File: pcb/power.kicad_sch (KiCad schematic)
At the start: 27 parts, among them IC3 XC6227C331MR-G, IC6 BQ24073RGTR, U3 CR2032-BS-6-1

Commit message: created step file
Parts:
- removed R27: DNF_0805, Resistor_SMD:R_0805_2012Metric_Pad1.20x1.40mm_HandSolder, symbol personal:DNF_0805
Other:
- note removed: "Charger Bypass"
- note removed: "Remove Charger 0 Ohm link first!"

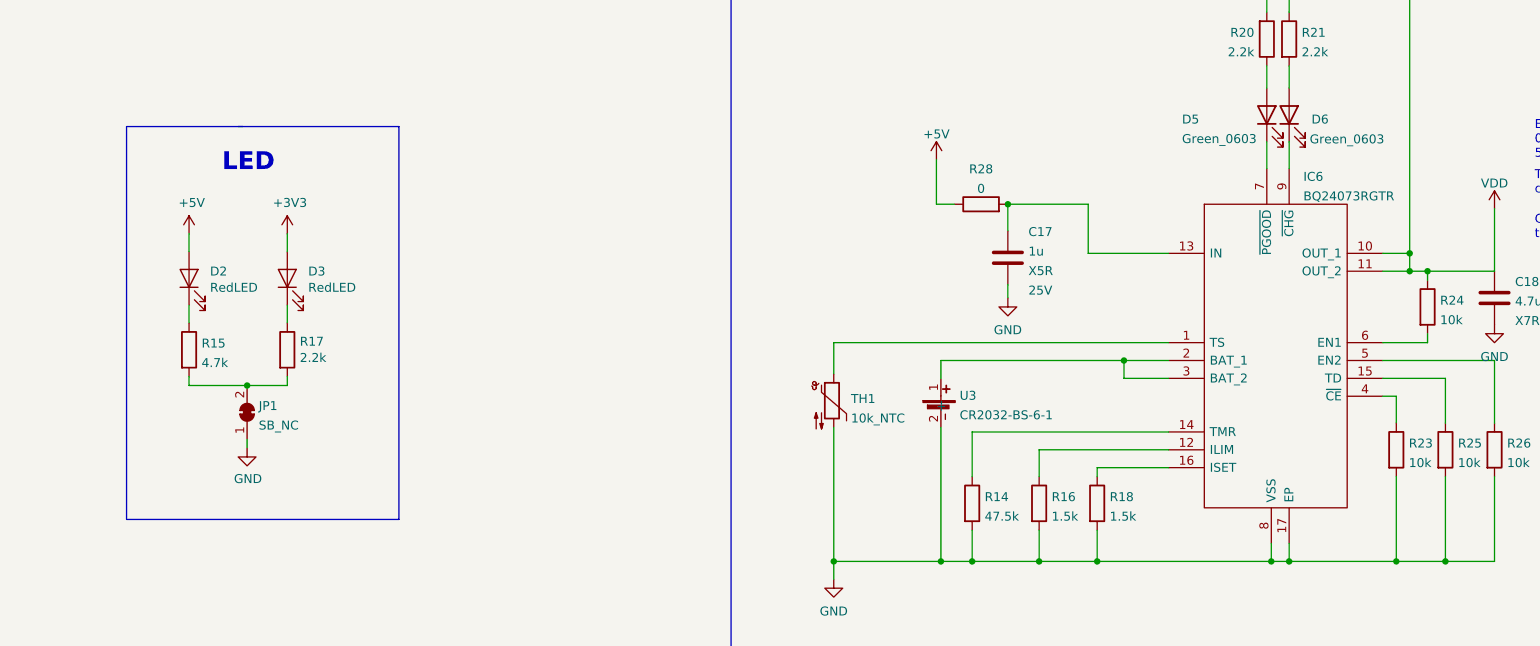
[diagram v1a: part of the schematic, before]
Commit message: Added demo scripts
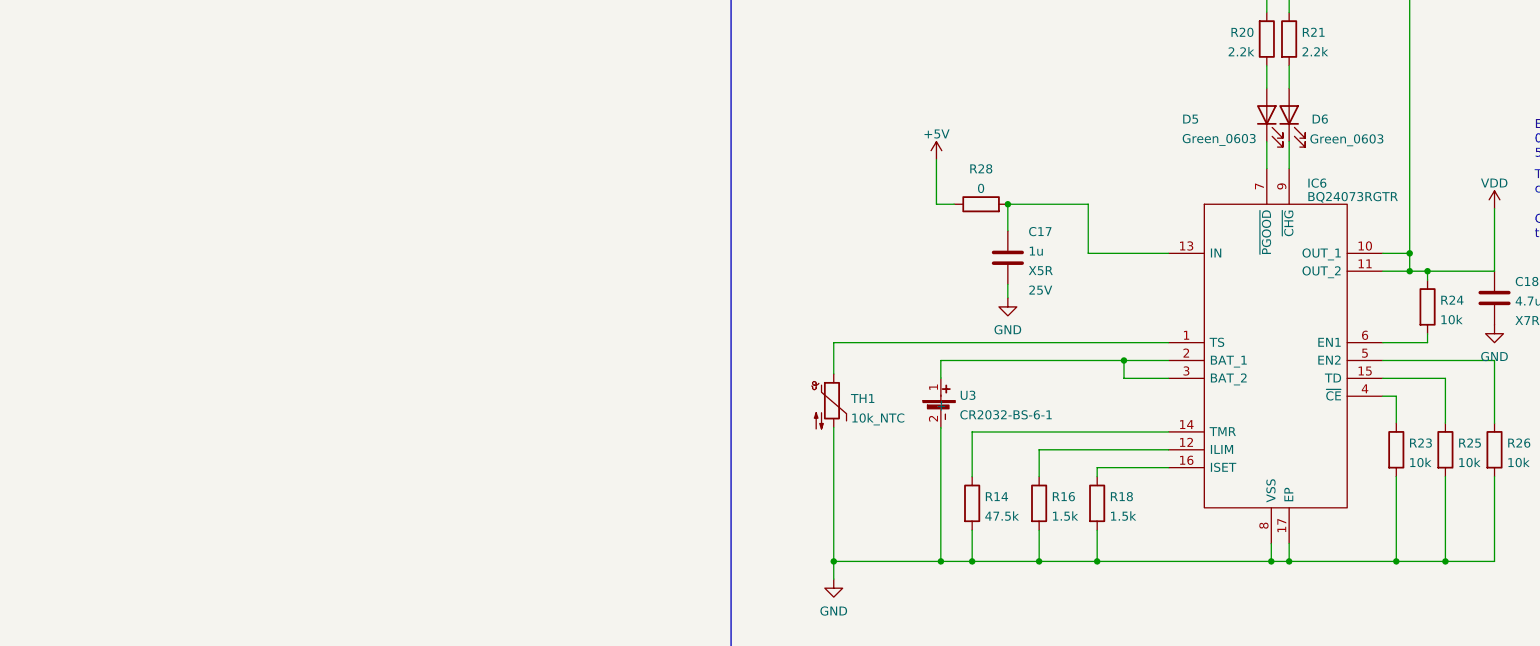
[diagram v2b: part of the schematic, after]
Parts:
- removed D2, D3: RedLED, Diode_SMD:D_0805_2012Metric, symbol Diode_JLC:RedLED
- removed JP1: SB_NC, Jumper:SolderJumper-2_P1.3mm_Bridged_Pad1.0x1.5mm, symbol personal:SB_NC
- removed R15: 4.7k, Resistor_SMD:R_0402_1005Metric, symbol Resistor_JLC:4.7k
- removed R17: 2.2k, Resistor_SMD:R_0402_1005Metric, symbol Resistor_JLC:2.2k
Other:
- note removed: "LED"

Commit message: Completed initial schematic
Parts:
- removed C10, C7: 10u, Capacitor_SMD:C_0805_2012Metric, symbol Capacitor_JLC:10u
- removed C17: 1u, Capacitor_SMD:C_0402_1005Metric, symbol Capacitor_JLC:1u
- removed C18: 4.7u, Capacitor_SMD:C_1206_3216Metric, symbol Capacitor_JLC:4.7u
- removed D5, D6: Green_0603, LED_SMD:LED_0603_1608Metric, symbol Diode_JLC:Green_0603
- removed IC3: XC6227C331MR-G, SOT95P280X130-5N, symbol Power-Drivers_JLC:XC6227C331MR-G
- removed IC6: BQ24073RGTR, QFN50P300X300X100-17N-D, symbol Power-Drivers_JLC:BQ24073RGTR
- removed R12: 100k, Resistor_SMD:R_0402_1005Metric, symbol Resistor_JLC:100k
- removed R14: 47.5k, Resistor_SMD:R_0402_1005Metric, symbol Resistor_JLC:47.5k
- removed R16, R18: 1.5k, Resistor_SMD:R_0402_1005Metric, symbol Resistor_JLC:1.5k
- removed R20, R21: 2.2k, Resistor_SMD:R_0402_1005Metric, symbol Resistor_JLC:2.2k
- removed R23, R24, R25, R26: 10k, Resistor_SMD:R_0402_1005Metric, symbol Resistor_JLC:10k
- removed R28: 0, Resistor_SMD:R_0805_2012Metric_Pad1.20x1.40mm_HandSolder, symbol Resistor_JLC:0
- removed TH1: 10k_NTC, Resistor_SMD:R_0402_1005Metric, symbol Resistor_JLC:10k_NTC
- removed U3: CR2032-BS-6-1, CR2032BS61, symbol BatteryHolder_JLC:CR2032-BS-6-1
- added C13, C15, C16: 10u, Capacitor_SMD:C_0805_2012Metric, symbol Capacitor_JLC:10u
- added C14: 1n, Capacitor_SMD:C_0402_1005Metric, symbol Capacitor_JLC:1n
- added IC5: TPS63051RMWR, QFN50P250X250X100-12N-D, symbol Power-Drivers_JLC:TPS63051RMWR
- added L1: 1.5uH, Inductor_SMD:L_0805_2012Metric, symbol Inductor_JLC:1.5uH
- added R16: 1M, Resistor_SMD:R_0402_1005Metric, symbol Resistor_JLC:1M
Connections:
- net GND: now also C13.2, C14.2, C15.2, C16.2, IC5.2 (GND_1), IC5.6 (PFM/PWM), IC5.9 (GND_2)
- net VDD: now also C13.1, IC5.10 (ILIM0), IC5.11 (EN), IC5.12 (VIN)
- new net: IC5.1 (L1), L1.1
- new net: IC5.3 (L2), L1.2
- new net: C14.1, IC5.7 (SS)
- new net: IC5.8 (PG), R16.2
- new net 3V3: C15.1, C16.1, IC5.4 (VOUT), IC5.5 (FB), R16.1
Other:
- note removed: "5V-3V3"
- note removed: "Battery Charger"
- note removed: "Connect ~CE to a low logic level to enable the battery charger"
- note removed: "EN2 EN1 0 1 500 mA. USB500 mode"
- note removed: "TD - Connect TD to VSS to enable charger termination."
